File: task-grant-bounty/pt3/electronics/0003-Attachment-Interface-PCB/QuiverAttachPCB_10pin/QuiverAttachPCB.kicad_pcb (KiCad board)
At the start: 2 copper layers, 24 x 16 mm, 3 parts, among them J1 2077601281, J2 813-22-010-30-000101, J3 419-10-210-30-054000

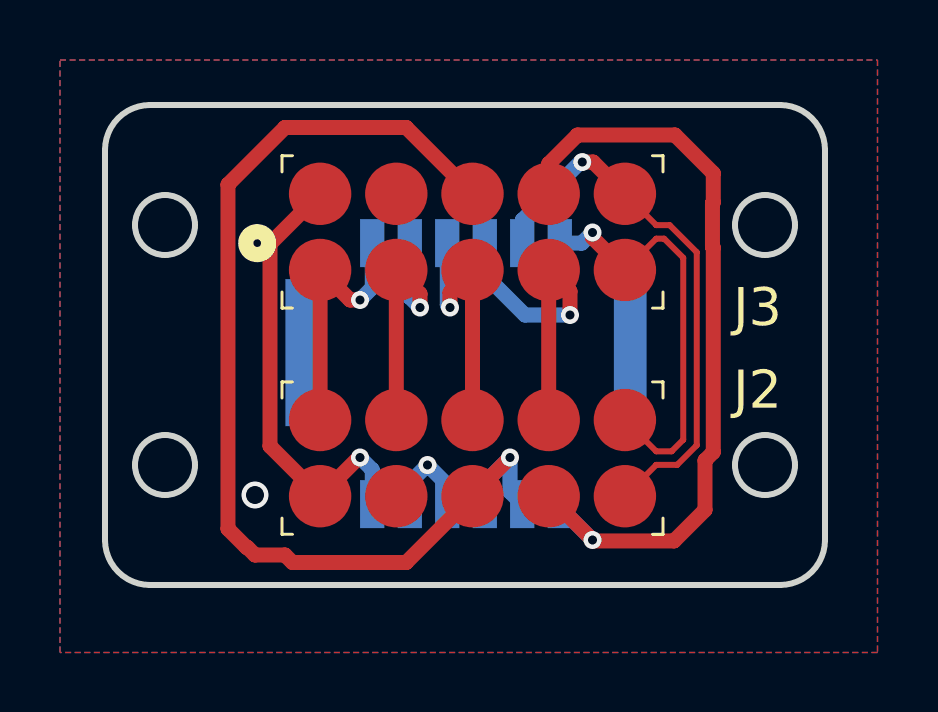
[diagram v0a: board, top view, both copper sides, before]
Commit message: Update PCB, docs based on feedbacl
- Update information note
- Change pin headers
- re-generate output files
- update images for documentation
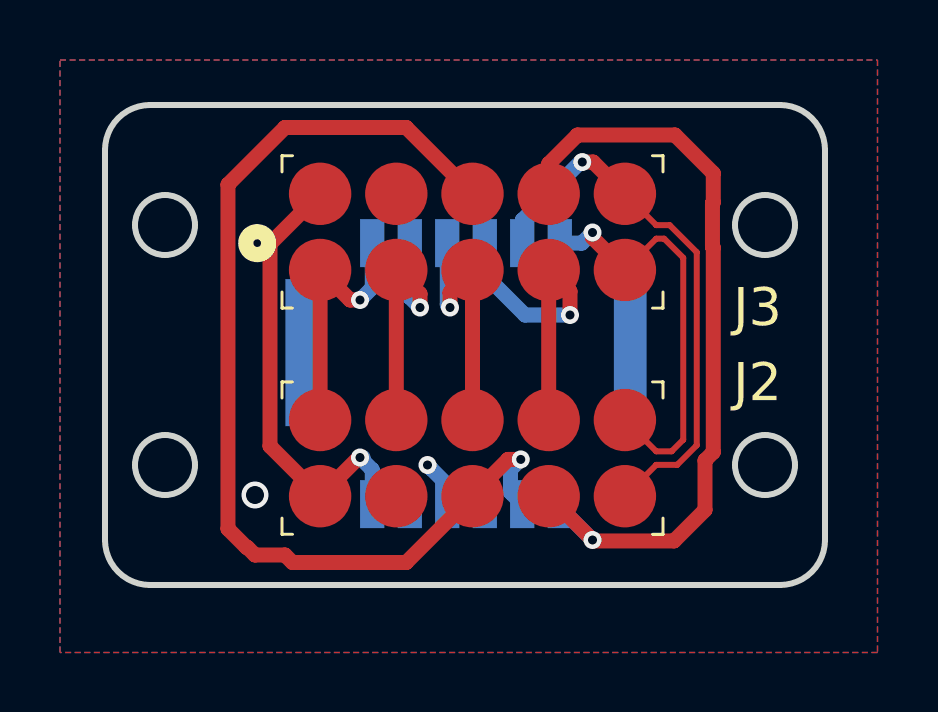
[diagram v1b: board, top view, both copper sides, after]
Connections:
- J1 pad 4: GND -> 12VSW
- J1 pad 8: +12V -> GND
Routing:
- net +12V: track 36.3 -> 34.8 mm
- net 12VSW: track 15.1 -> 16.4 mm
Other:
- board text added: "v1.1"
- board text removed: "v1"
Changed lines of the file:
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@@
 		(tags "Connector")
 		(property "Reference" "J2"
-			(at 9.5 -2.04 0)
+			(at 9.5 -2.29 0)
 			(layer "F.SilkS")
 			(effects
@@
 			(size 0.8128 1.6002)
 			(layers "B.Cu" "B.Mask" "B.Paste")
-			(net 1 "GND")
+			(net 3 "12VSW")
 			(pinfunction "4")
 			(pintype "unspecified")
@@
 			(size 0.8128 1.6002)
 			(layers "B.Cu" "B.Mask" "B.Paste")
-			(net 8 "+12V")
+			(net 1 "GND")
 			(pinfunction "8")
 			(pintype "unspecified")
@@
 		(layer "Edge.Cuts")
 	)
-	(gr_text "v1"
-		(at 120.25 131.5 90)
+	(gr_text "v1.1\n"
+		(at 120.5 130.75 90)
 		(layer "B.SilkS")
 		(effects
@@
 	)
 	(segment
+		(start 110.6584 138.304852)
+		(end 110.054852 138.304852)
+		(width 0.5)
+		(layer "B.Cu")
+		(net 1)
+	)
+	(segment
+		(start 109.4084 138.304852)
+		(end 110.6584 138.304852)
+		(width 0.5)
+		(layer "B.Cu")
+		(net 1)
+	)
+	(segment
+		(start 108.875 137.125)
+		(end 108.75 137)
+		(width 0.5)
+		(layer "B.Cu")
+		(net 1)
+	)
+	(segment
 		(start 109.4084 137.6584)
-		(end 108.75 137)
+		(end 108.875 137.125)
 		(width 0.5)
 		(layer "B.Cu")
@@
 		(start 109.4084 138.304852)
 		(end 109.4084 137.6584)
-		(width 0.5)
-		(layer "B.Cu")
-		(net 1)
-	)
-	(segment
-		(start 108.1584 137.5916)
-		(end 108.75 137)
-		(width 0.5)
-		(layer "B.Cu")
-		(net 1)
-	)
-	(segment
-		(start 108.1584 138.304852)
-		(end 108.1584 137.5916)
 		(width 0.5)
 		(layer "B.Cu")
@@
 	)
 	(segment
+		(start 106.603548 136.75)
+		(end 106.5 136.75)
+		(width 0.5)
+		(layer "B.Cu")
+		(net 3)
+	)
+	(segment
+		(start 106.9084 138.304852)
+		(end 108.1584 138.304852)
+		(width 0.5)
+		(layer "B.Cu")
+		(net 3)
+	)
+	(segment
 		(start 113.5 132)
 		(end 113.5 131.21)
@@
 	)
 	(segment
-		(start 110.25 138)
-		(end 111.5 136.75)
-		(width 0.5)
-		(layer "F.Cu")
-		(net 8)
-	)
-	(segment
 		(start 102.720777 139.75)
 		(end 102.099 139.128223)
@@
 	)
 	(segment
+		(start 111.858469 136.813681)
+		(end 111.436319 136.813681)
+		(width 0.5)
+		(layer "F.Cu")
+		(net 8)
+	)
+	(segment
+		(start 111.436319 136.813681)
+		(end 110.25 138)
+		(width 0.5)
+		(layer "F.Cu")
+		(net 8)
+	)
+	(segment
 		(start 102.75 139.75)
 		(end 102.720777 139.75)
@@
 	)
 	(segment
+		(start 110.25 138)
+		(end 110.25 138.04)
+		(width 0.5)
+		(layer "F.Cu")
+		(net 8)
+	)
+	(segment
 		(start 110.25 138.04)
 		(end 108.04 140.25)
@@
 	)
 	(segment
-		(start 110.25 138.04)
-		(end 110.25 138)
-		(width 0.5)
-		(layer "F.Cu")
-		(net 8)
-	)
-	(segment
 		(start 104 125.75)
 		(end 108.04 125.75)
@@
 	)
 	(via
-		(at 111.5 136.75)
+		(at 111.858469 136.813681)
 		(size 0.6)
 		(drill 0.3)
@@
 	)
 	(segment
-		(start 111.5 137.896452)
+		(start 111.858469 136.813681)
+		(end 111.5158 137.15635)
+		(width 0.5)
+		(layer "B.Cu")
+		(net 8)
+	)
+	(segment
+		(start 111.5158 137.15635)
+		(end 111.5158 137.912252)
+		(width 0.5)
+		(layer "B.Cu")
+		(net 8)
+	)
+	(segment
+		(start 111.5158 137.912252)
 		(end 111.9084 138.304852)
 		(width 0.5)
 		(layer "B.Cu")
-		(net 8)
-	)
-	(segment
-		(start 110.6584 138.304852)
-		(end 110.6584 137.5916)
-		(width 0.5)
-		(layer "B.Cu")
-		(net 8)
-	)
-	(segment
-		(start 111.5 136.75)
-		(end 111.5 137.896452)
-		(width 0.5)
-		(layer "B.Cu")
-		(net 8)
-	)
-	(segment
-		(start 110.6584 137.5916)
-		(end 111.5 136.75)
-		(width 0.5)
-		(layer "B.Cu")

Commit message: Center molex, adjust edges
v 1.2
- Centered molex header between mounting holes
- Adjusted edge dimensions to 23.5mm x 15.8mm
- Brought in corners to 2mm chamfered
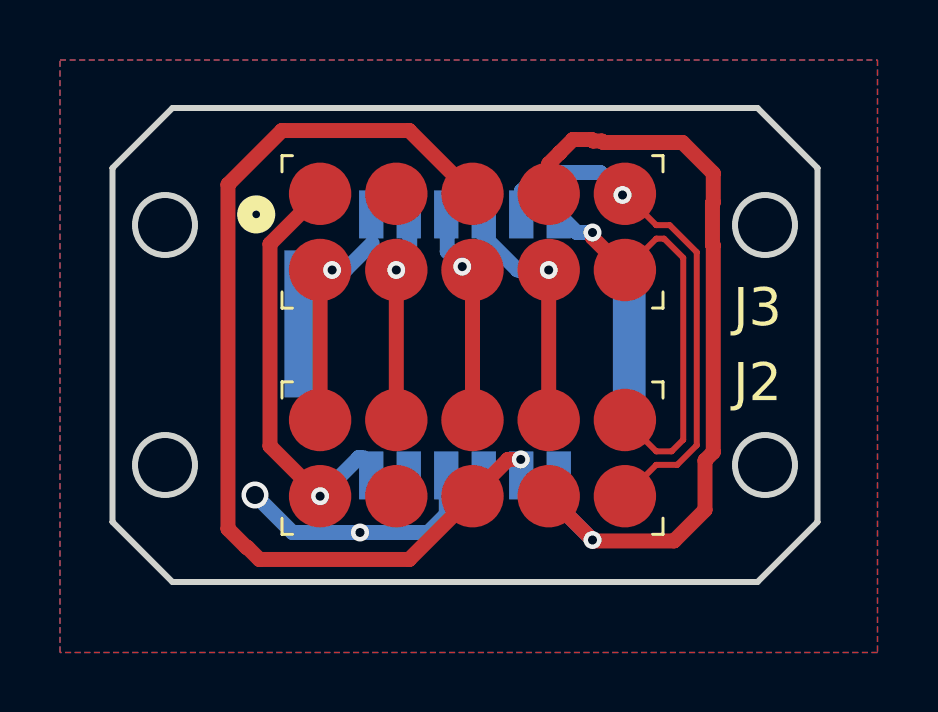
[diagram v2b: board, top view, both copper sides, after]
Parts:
- moved J1 0.96 mm to (110.0, 133.0)
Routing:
- net GND: track 3.43 -> 9.79 mm
- net ETH_TX-: track 11.2 -> 8.36 mm
- net +12V: track 34.8 -> 32.8 mm
- net ETH_RX-: track 8.92 -> 7.05 mm
- net ETH_RX+: track 8.87 -> 7.11 mm
- net 12VSW: track 16.4 -> 14.7 mm
- net ETH_TX+: track 8.80 -> 7.35 mm
- net FMU_CH1: track 27.4 -> 26.6 mm
- net CAN1_N: track 18.2 -> 17.5 mm
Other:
- board size 24 x 16 mm -> 23.5 x 15.8 mm
- board text added: "2025-07-31"
- board text added: "v1.2"
- board text removed: "2025-06-02"
- board text removed: "v1.1"
